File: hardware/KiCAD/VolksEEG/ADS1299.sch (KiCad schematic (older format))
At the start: 18 parts, among them U1 ADS1299IPAG

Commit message: Added Digi-key's kicad component libraries, some work done on power, think this will change but capturing it here for posterity.
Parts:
- removed C? (x4): 100n, symbol Device:C
- removed C? (x6): 1u, symbol Device:C
- removed R?: 10k, symbol Device:R
- added C? (x2): 100n, symbol Device:C
- added C? (x4): 1u, symbol Device:C
- added C?: 0.1u, symbol Device:C
- added C?: 10u, symbol Device:C
- added R? (x2): ?, symbol Device:R
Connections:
- net labels added: +2V5, -2V5, MISO_ads, MOSI_ads, SCK_ads, nCS_ads, nDRDY_ads
- net labels removed: MISO, MOSI, SCK, nCS
- wire segments 107 -> 91

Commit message: Updating analogue inputs to the referential montage and connected a few ADS1299 pins.
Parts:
- added R? (x2): 10K, symbol Device:R
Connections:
- net labels added: AIN1, AIN2, AIN3, AIN4, AIN5, AIN6, AIN7, AIN8, BIAS_INV, BIAS_OUT, REF, VDD
- net labels removed: AIN1N, AIN1P, AIN2N, AIN2P, AIN3N, AIN3P, AIN4N, AIN4P, AIN5N, AIN5P, AIN6N, AIN6P, AIN7N, AIN7P, AIN8N, AIN8P
- wire segments 91 -> 110
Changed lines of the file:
@@
 Wire Wire Line
 	5550 4250 6000 4250
-Text HLabel 3550 1500 0    50   Input ~ 0
+Text HLabel 3500 1500 0    50   Input ~ 0
 ADS-nRST
-Text HLabel 3500 3250 0    50   Input ~ 0
-AIN5N
 Text HLabel 3500 3350 0    50   Input ~ 0
-AIN5P
-Text HLabel 3500 3450 0    50   Input ~ 0
-AIN6N
+AIN5
 Text HLabel 3500 3550 0    50   Input ~ 0
-AIN6P
-Text HLabel 3500 3650 0    50   Input ~ 0
-AIN7N
+AIN6
 Text HLabel 3500 3750 0    50   Input ~ 0
-AIN7P
-Text HLabel 3500 3850 0    50   Input ~ 0
-AIN8N
+AIN7
 Text HLabel 3500 3950 0    50   Input ~ 0
-AIN8P
+AIN8
 Wire Wire Line
 	3500 4250 4150 4250
@@
 	4150 3950 3500 3950
 Wire Wire Line
-	4150 3850 3500 3850
-Wire Wire Line
 	4150 3750 3500 3750
 Wire Wire Line
-	4150 3650 3500 3650
-Wire Wire Line
 	3500 3550 4150 3550
 Wire Wire Line
-	4150 3450 3500 3450
-Wire Wire Line
 	3500 3350 4150 3350
-Wire Wire Line
-	4150 3250 3500 3250
-Text HLabel 3500 2450 0    50   Input ~ 0
-AIN1N
 Text HLabel 3500 2550 0    50   Input ~ 0
-AIN1P
-Text HLabel 3500 2650 0    50   Input ~ 0
-AIN2N
+AIN1
 Text HLabel 3500 2750 0    50   Input ~ 0
-AIN2P
-Text HLabel 3500 2850 0    50   Input ~ 0
-AIN3N
+AIN2
 Text HLabel 3500 2950 0    50   Input ~ 0
-AIN3P
-Text HLabel 3500 3050 0    50   Input ~ 0
-AIN4N
+AIN3
 Text HLabel 3500 3150 0    50   Input ~ 0
-AIN4P
+AIN4
 Wire Wire Line
 	4150 3150 3500 3150
 Wire Wire Line
-	4150 3050 3500 3050
-Wire Wire Line
 	4150 2950 3500 2950
 Wire Wire Line
-	4150 2850 3500 2850
-Wire Wire Line
 	3500 2750 4150 2750
 Wire Wire Line
-	4150 2650 3500 2650
-Wire Wire Line
 	3500 2550 4150 2550
-Wire Wire Line
-	4150 2450 3500 2450
 Wire Wire Line
 	5550 1750 5550 1650
@@
 Text HLabel 6800 2250 2    50   Output ~ 0
 nDRDY_ads
-$Comp
-L power:+3V3 #PWR?
-U 1 1 617DA57B
-P 6650 1500
-F 0 "#PWR?" H 6650 1350 50  0001 C CNN
-F 1 "+3V3" V 6665 1628 50  0000 L CNN
-F 2 "" H 6650 1500 50  0001 C CNN
-F 3 "" H 6650 1500 50  0001 C CNN
-	1    6650 1500
-	1    0    0    -1
-$EndComp
 Wire Wire Line
 	5900 2000 5900 1800
@@
 Connection ~ 6650 2250
 Wire Wire Line
-	3550 1500 4150 1500
+	3500 1500 4150 1500
 Wire Wire Line
 	6650 1500 6650 1600
@@
 Text HLabel 6550 6000 2    50   Input ~ 0
 -2V5
+$Comp
+L power:VDD #PWR?
+U 1 1 61A7B2BC
+P 6650 1500
+AR Path="/615BA255/61A7B2BC" Ref="#PWR?"  Part="1"
+AR Path="/615BA110/61A7B2BC" Ref="#PWR?"  Part="1"
+F 0 "#PWR?" H 6650 1350 50  0001 C CNN
+F 1 "VDD" H 6665 1673 50  0000 C CNN
+F 2 "" H 6650 1500 50  0001 C CNN
+F 3 "" H 6650 1500 50  0001 C CNN
+	1    6650 1500
+	1    0    0    -1
+$EndComp
+$Comp
+L Device:R R?
+U 1 1 61A7F38E
+P 3850 1750
+F 0 "R?" V 3950 1650 50  0000 L CNN
+F 1 "10K" V 3950 1800 50  0000 L CNN
+F 2 "" V 3780 1750 50  0001 C CNN
+F 3 "~" H 3850 1750 50  0001 C CNN
+	1    3850 1750
+	0    -1   -1   0
+$EndComp
+$Comp
+L power:VDD #PWR?
+U 1 1 61A7F869
+P 2750 1550
+AR Path="/615BA255/61A7F869" Ref="#PWR?"  Part="1"
+AR Path="/615BA110/61A7F869" Ref="#PWR?"  Part="1"
+F 0 "#PWR?" H 2750 1400 50  0001 C CNN
+F 1 "VDD" H 2765 1723 50  0000 C CNN
+F 2 "" H 2750 1550 50  0001 C CNN
+F 3 "" H 2750 1550 50  0001 C CNN
+	1    2750 1550
+	1    0    0    -1
+$EndComp
+Wire Wire Line
+	2750 1550 2750 1750
+Wire Wire Line
+	2750 1750 3700 1750
+Wire Wire Line
+	4000 1750 4150 1750
+Text HLabel 5850 2350 2    50   Output ~ 0
+BIAS_OUT
+Text HLabel 3500 2100 0    50   Output ~ 0
+BIAS_INV
+Wire Wire Line
+	3500 2100 4150 2100
+Wire Wire Line
+	5550 2350 5850 2350
+$Comp
+L Device:R R?
+U 1 1 61AF48E0
+P 3850 1400
+F 0 "R?" V 3950 1300 50  0000 L CNN
+F 1 "10K" V 3950 1450 50  0000 L CNN
+F 2 "" V 3780 1400 50  0001 C CNN
+F 3 "~" H 3850 1400 50  0001 C CNN
+	1    3850 1400
+	0    -1   -1   0
+$EndComp
+$Comp
+L power:VDD #PWR?
+U 1 1 61AF7617
+P 3500 1200
+AR Path="/615BA255/61AF7617" Ref="#PWR?"  Part="1"
+AR Path="/615BA110/61AF7617" Ref="#PWR?"  Part="1"
+F 0 "#PWR?" H 3500 1050 50  0001 C CNN
+F 1 "VDD" H 3515 1373 50  0000 C CNN
+F 2 "" H 3500 1200 50  0001 C CNN
+F 3 "" H 3500 1200 50  0001 C CNN
+	1    3500 1200
+	1    0    0    -1
+$EndComp
+Wire Wire Line
+	3500 1200 3500 1400
+Wire Wire Line
+	3500 1400 3700 1400
+Wire Wire Line
+	4000 1400 4150 1400
+Text HLabel 3500 5600 0    50   Input ~ 0
+REF
+Wire Wire Line
+	3500 5600 4150 5600
+$Comp
+L power:VDD #PWR?
+U 1 1 61B0BA08
+P 2750 2400
+AR Path="/615BA255/61B0BA08" Ref="#PWR?"  Part="1"
+AR Path="/615BA110/61B0BA08" Ref="#PWR?"  Part="1"
+F 0 "#PWR?" H 2750 2250 50  0001 C CNN
+F 1 "VDD" H 2765 2573 50  0000 C CNN
+F 2 "" H 2750 2400 50  0001 C CNN
+F 3 "" H 2750 2400 50  0001 C CNN
+	1    2750 2400
+	1    0    0    -1
+$EndComp
+Wire Wire Line
+	2750 2400 2750 2450
+Wire Wire Line
+	2750 3850 4150 3850
+Wire Wire Line
+	4150 3650 2750 3650
+Connection ~ 2750 3650
+Wire Wire Line
+	2750 3650 2750 3850
+Wire Wire Line
+	4150 3450 2750 3450
+Connection ~ 2750 3450
+Wire Wire Line
+	2750 3450 2750 3650
+Wire Wire Line
+	2750 3250 4150 3250
+Connection ~ 2750 3250
+Wire Wire Line
+	2750 3250 2750 3450
+Wire Wire Line
+	4150 3050 2750 3050
+Connection ~ 2750 3050
+Wire Wire Line
+	2750 3050 2750 3250
+Wire Wire Line
+	2750 2850 4150 2850
+Connection ~ 2750 2850
+Wire Wire Line
+	2750 2850 2750 3050
+Wire Wire Line
+	2750 2650 4150 2650
+Connection ~ 2750 2650
+Wire Wire Line
+	2750 2650 2750 2850
+Wire Wire Line
+	2750 2450 4150 2450
+Connection ~ 2750 2450
+Wire Wire Line
+	2750 2450 2750 2650
+$Comp
+L power:GNDA #PWR?
+U 1 1 61B27A78
+P 2950 1950
+F 0 "#PWR?" H 2950 1700 50  0001 C CNN
+F 1 "GNDA" H 2955 1777 50  0000 C CNN
+F 2 "" H 2950 1950 50  0001 C CNN
+F 3 "" H 2950 1950 50  0001 C CNN
+	1    2950 1950
+	1    0    0    -1
+$EndComp
+Wire Wire Line
+	2950 1950 2950 1850
+Wire Wire Line
+	2950 1850 4150 1850
 $EndSCHEMATC

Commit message: Updated names of heirarchical pins, finished referential montage configuration, added filter cap to ADS_nRST line, started putting ADS1299 gpios to a header.
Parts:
- removed U?: OPA388IDGKR, VolksEEG:SOP65P490X110-8N, symbol VolksEEG:OPA388IDGKR
- added C?: 100n, symbol Device:C
- added R?: 10K, symbol Device:R
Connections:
- net labels added: ADS_nDRDY, ADS_nRST, MISO, MOSI, SCK, nCS
- net labels removed: ADS-nRST, MISO_ads, MOSI_ads, SCK_ads, nCS_ads, nDRDY_ads
- wire segments 110 -> 125
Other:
- moved on the sheet: R?
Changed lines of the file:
@@
 $EndComp
 Text HLabel 3500 4250 0    50   Input ~ 0
-nCS_ads
+nCS
 Text HLabel 3500 4350 0    50   Input ~ 0
-SCK_ads
+SCK
 Text HLabel 3500 4450 0    50   Input ~ 0
-MOSI_ads
+MOSI
 Text HLabel 6000 4250 2    50   Output ~ 0
-MISO_ads
+MISO
 Wire Wire Line
 	5550 4250 6000 4250
-Text HLabel 3500 1500 0    50   Input ~ 0
-ADS-nRST
+Text HLabel 3300 1500 0    50   Input ~ 0
+ADS_nRST
 Text HLabel 3500 3350 0    50   Input ~ 0
 AIN5
@@
 Wire Wire Line
 	7500 5400 7500 5300
-$Comp
-L VolksEEG:OPA388IDGKR U?
-U 1 1 617AA68D
-P 8650 3600
-F 0 "U?" H 8994 3646 50  0000 L CNN
-F 1 "OPA388IDGKR" H 8994 3555 50  0000 L CNN
-F 2 "VolksEEG:SOP65P490X110-8N" H 8650 3600 50  0001 C CNN
-F 3 "https://www.ti.com/lit/gpn/opa388" H 8650 3600 50  0001 C CNN
-	1    8650 3600
-	1    0    0    -1
-$EndComp
 Wire Wire Line
 	5550 2550 5700 2550
@@
 $EndComp
 Text HLabel 6800 2250 2    50   Output ~ 0
-nDRDY_ads
+ADS_nDRDY
 Wire Wire Line
 	5900 2000 5900 1800
@@
 Connection ~ 6650 2250
 Wire Wire Line
-	3500 1500 4150 1500
+	3300 1500 3550 1500
 Wire Wire Line
 	6650 1500 6650 1600
@@
 L Device:R R?
 U 1 1 61A7F38E
-P 3850 1750
-F 0 "R?" V 3950 1650 50  0000 L CNN
-F 1 "10K" V 3950 1800 50  0000 L CNN
-F 2 "" V 3780 1750 50  0001 C CNN
-F 3 "~" H 3850 1750 50  0001 C CNN
-	1    3850 1750
-	0    -1   -1   0
-$EndComp
-$Comp
-L power:VDD #PWR?
-U 1 1 61A7F869
-P 2750 1550
-AR Path="/615BA255/61A7F869" Ref="#PWR?"  Part="1"
-AR Path="/615BA110/61A7F869" Ref="#PWR?"  Part="1"
-F 0 "#PWR?" H 2750 1400 50  0001 C CNN
-F 1 "VDD" H 2765 1723 50  0000 C CNN
-F 2 "" H 2750 1550 50  0001 C CNN
-F 3 "" H 2750 1550 50  0001 C CNN
-	1    2750 1550
-	1    0    0    -1
-$EndComp
-Wire Wire Line
-	2750 1550 2750 1750
-Wire Wire Line
-	2750 1750 3700 1750
-Wire Wire Line
-	4000 1750 4150 1750
+P 4050 1000
+F 0 "R?" V 4150 900 50  0000 L CNN
+F 1 "10K" V 4150 1050 50  0000 L CNN
+F 2 "" V 3980 1000 50  0001 C CNN
+F 3 "~" H 4050 1000 50  0001 C CNN
+	1    4050 1000
+	-1   0    0    1
+$EndComp
 Text HLabel 5850 2350 2    50   Output ~ 0
 BIAS_OUT
@@
 L Device:R R?
 U 1 1 61AF48E0
-P 3850 1400
-F 0 "R?" V 3950 1300 50  0000 L CNN
-F 1 "10K" V 3950 1450 50  0000 L CNN
-F 2 "" V 3780 1400 50  0001 C CNN
-F 3 "~" H 3850 1400 50  0001 C CNN
-	1    3850 1400
-	0    -1   -1   0
+P 3800 1000
+F 0 "R?" V 3900 900 50  0000 L CNN
+F 1 "10K" V 3900 1050 50  0000 L CNN
+F 2 "" V 3730 1000 50  0001 C CNN
+F 3 "~" H 3800 1000 50  0001 C CNN
+	1    3800 1000
+	-1   0    0    1
 $EndComp
 $Comp
 L power:VDD #PWR?
 U 1 1 61AF7617
-P 3500 1200
+P 3800 700
 AR Path="/615BA255/61AF7617" Ref="#PWR?"  Part="1"
 AR Path="/615BA110/61AF7617" Ref="#PWR?"  Part="1"
-F 0 "#PWR?" H 3500 1050 50  0001 C CNN
-F 1 "VDD" H 3515 1373 50  0000 C CNN
-F 2 "" H 3500 1200 50  0001 C CNN
-F 3 "" H 3500 1200 50  0001 C CNN
-	1    3500 1200
-	1    0    0    -1
-$EndComp
-Wire Wire Line
-	3500 1200 3500 1400
-Wire Wire Line
-	3500 1400 3700 1400
-Wire Wire Line
-	4000 1400 4150 1400
+F 0 "#PWR?" H 3800 550 50  0001 C CNN
+F 1 "VDD" H 3815 873 50  0000 C CNN
+F 2 "" H 3800 700 50  0001 C CNN
+F 3 "" H 3800 700 50  0001 C CNN
+	1    3800 700
+	1    0    0    -1
+$EndComp
 Text HLabel 3500 5600 0    50   Input ~ 0
 REF
@@
 	2950 1950 2950 1850
 Wire Wire Line
-	2950 1850 4150 1850
+	2950 1850 3550 1850
+Entry Wire Line
+	3950 5450 4050 5350
+Entry Wire Line
+	3850 5450 3950 5350
+Entry Wire Line
+	3750 5450 3850 5350
+Entry Wire Line
+	3650 5450 3750 5350
+Wire Wire Line
+	4050 5350 4150 5350
+Wire Wire Line
+	4150 5250 4050 5250
+Wire Wire Line
+	4050 5250 3950 5350
+Wire Wire Line
+	4050 5150 3850 5350
+Wire Wire Line
+	4150 5150 4050 5150
+Wire Wire Line
+	3750 5350 4050 5050
+Wire Wire Line
+	4050 5050 4150 5050
+$Comp
+L Device:R R?
+U 1 1 61B84C6B
+P 3550 1000
+F 0 "R?" V 3650 900 50  0000 L CNN
+F 1 "10K" V 3650 1050 50  0000 L CNN
+F 2 "" V 3480 1000 50  0001 C CNN
+F 3 "~" H 3550 1000 50  0001 C CNN
+	1    3550 1000
+	-1   0    0    1
+$EndComp
+Wire Wire Line
+	3550 850  3550 750
+Wire Wire Line
+	3550 750  3800 750
+Wire Wire Line
+	3800 750  3800 700
+Wire Wire Line
+	3800 850  3800 750
+Connection ~ 3800 750
+Wire Wire Line
+	4050 850  4050 750
+Wire Wire Line
+	4050 750  3800 750
+Wire Wire Line
+	3550 1150 3550 1500
+Connection ~ 3550 1500
+Wire Wire Line
+	3550 1500 4150 1500
+Wire Wire Line
+	4050 1150 4050 1400
+Wire Wire Line
+	4050 1400 4150 1400
+Wire Wire Line
+	3800 1150 3800 1750
+Wire Wire Line
+	3800 1750 4150 1750
+$Comp
+L Device:C C?
+U 1 1 61B9DFC8
+P 3550 1650
+AR Path="/615BA110/61B9DFC8" Ref="C?"  Part="1"
+AR Path="/615BA255/61B9DFC8" Ref="C?"  Part="1"
+F 0 "C?" V 3700 1750 50  0000 L CNN
+F 1 "100n" V 3700 1500 50  0000 L CNN
+F 2 "" H 3588 1500 50  0001 C CNN
+F 3 "~" H 3550 1650 50  0001 C CNN
+	1    3550 1650
+	-1   0    0    1
+$EndComp
+Wire Wire Line
+	3550 1800 3550 1850
+Wire Bus Line
+	1650 5450 3950 5450
+Connection ~ 3550 1850
+Wire Wire Line
+	3550 1850 4150 1850
 $EndSCHEMATC

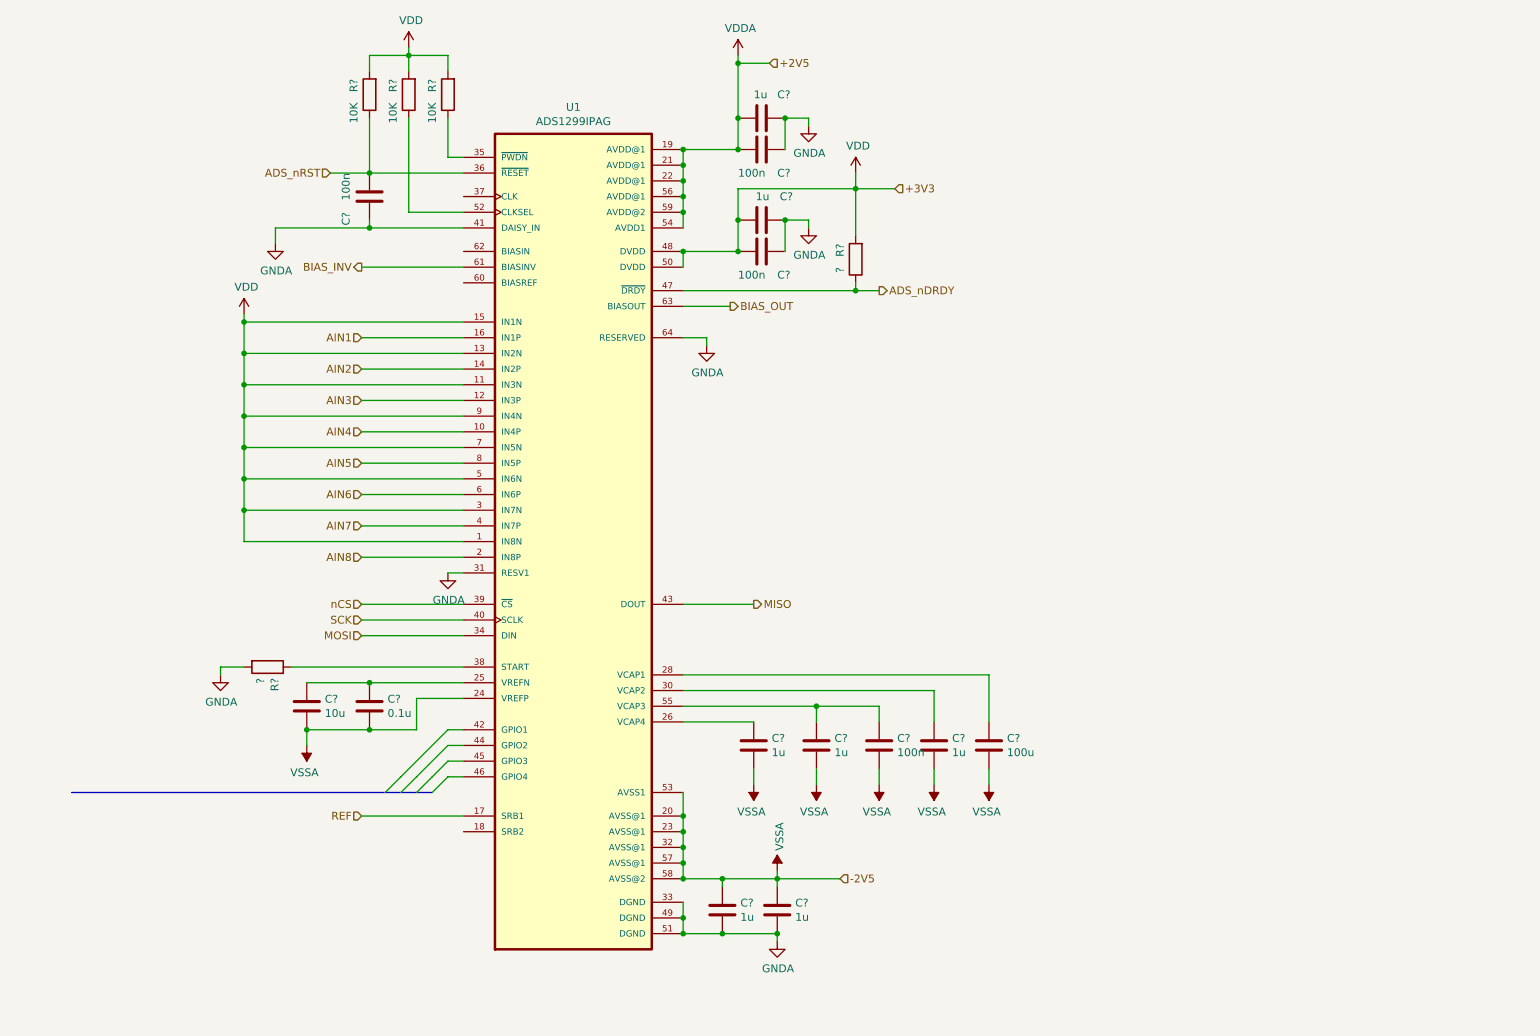
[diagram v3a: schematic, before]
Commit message: Added custom power symbols for non isolated power. Seperated Analogue and digital supplies. finished putting the ADS1299 GPIOs to a header.
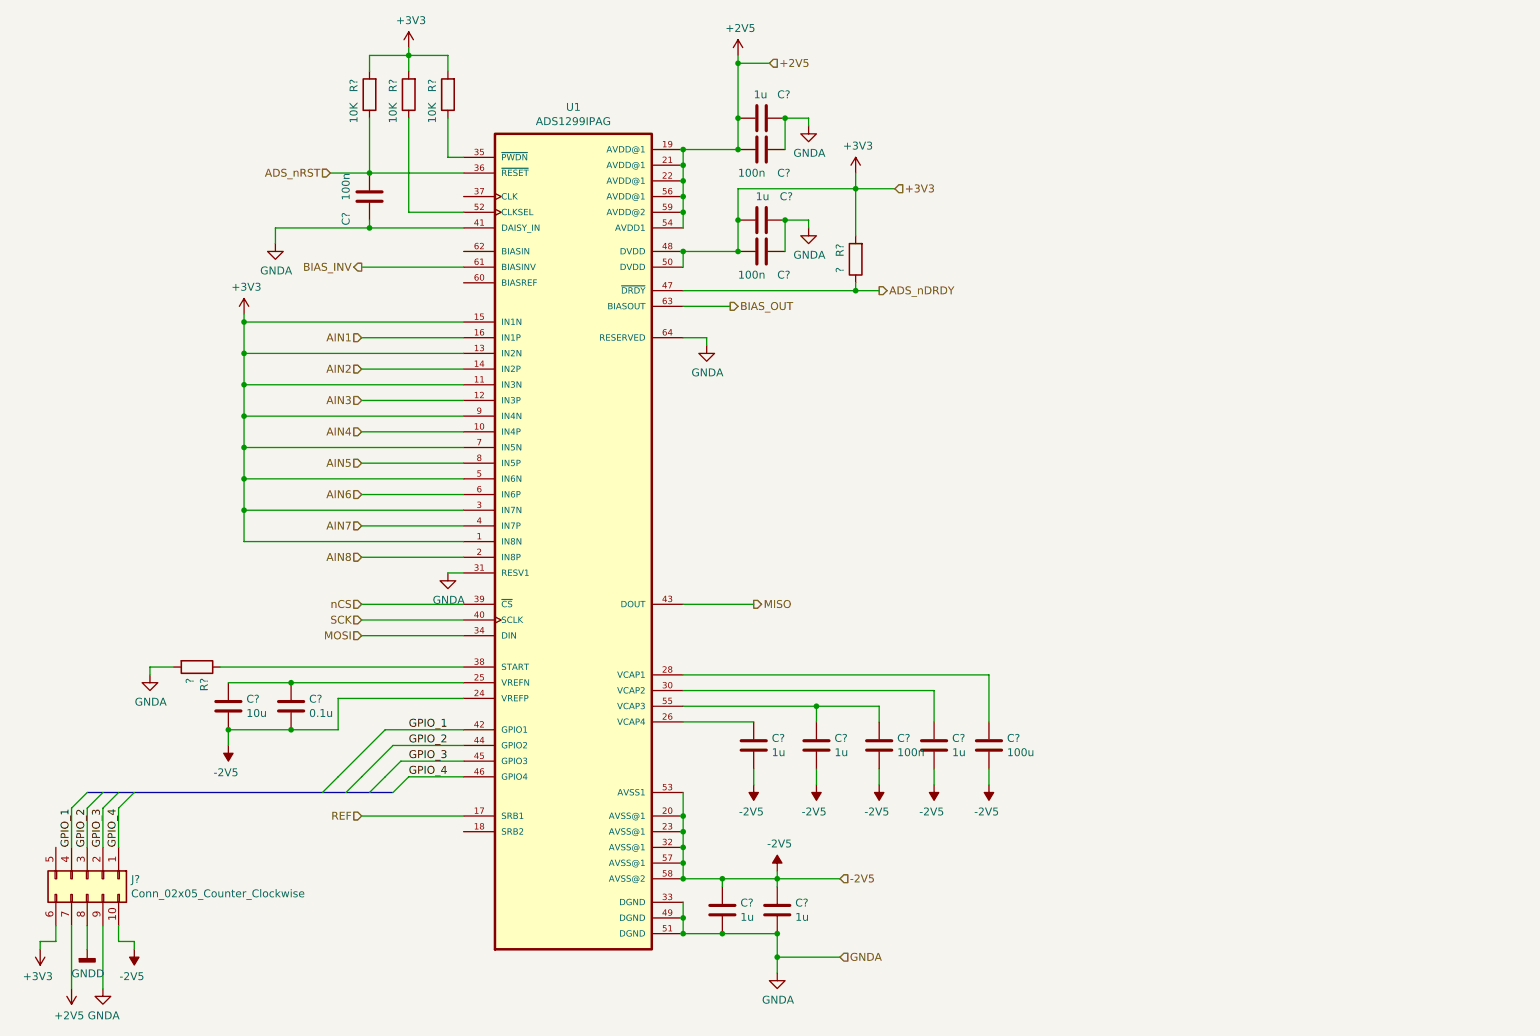
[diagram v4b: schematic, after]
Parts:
- added J?: Conn_02x05_Counter_Clockwise, symbol Connector_Generic:Conn_02x05_Counter_Clockwise
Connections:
- net GNDA: now also J?.9 (Pin_9)
- net GPIO_1: now reaches U1.42 (GPIO1)
- net GPIO_1: now also J?.4 (Pin_4)
- net GPIO_2: now reaches U1.44 (GPIO2)
- net GPIO_2: now also J?.3 (Pin_3)
- net GPIO_3: now reaches U1.45 (GPIO3)
- net GPIO_3: now also J?.2 (Pin_2)
- net GPIO_4: now reaches U1.46 (GPIO4)
- net GPIO_4: now also J?.1 (Pin_1)
- net VDD renamed +3V3
- net +3V3: now also J?.6 (Pin_6)
- net VDDA renamed +2V5
- net +2V5: now also J?.7 (Pin_7)
- net VSSA renamed -2V5
- net -2V5: now also J?.10 (Pin_10)
- new net GNDD: J?.8 (Pin_8)
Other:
- moved on the sheet: C?, R?

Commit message: Tweaks based on feedback, Changed digital isolators to ADUM240E devices due to component availability.
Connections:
- net GNDD is gone; now on net GNDA: J?.8 (Pin_8)
- net +2V5: now also U1.1 (IN8N), U1.11 (IN3N), U1.13 (IN2N), U1.15 (IN1N), U1.3 (IN7N), U1.5 (IN6N), U1.7 (IN5N), U1.9 (IN4N)
- net +3V3: no longer U1.1 (IN8N), U1.11 (IN3N), U1.13 (IN2N), U1.15 (IN1N), U1.3 (IN7N), U1.5 (IN6N), U1.7 (IN5N), U1.9 (IN4N)
- net -2V5: now also C?.1, C?.1, U1.25 (VREFN); no longer C?.2, C?.2, U1.24 (VREFP)
- new net: C?.2, C?.2, U1.24 (VREFP)
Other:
- moved on the sheet: R?
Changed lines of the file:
@@
 $Descr A4 11693 8268
 encoding utf-8
-Sheet 2 6
+Sheet 6 6
 Title ""
 Date ""
@@
 L Device:R R?
 U 1 1 61760E4E
-P 2450 4650
-F 0 "R?" H 2520 4696 50  0000 L CNN
-F 1 "?" H 2520 4605 50  0000 L CNN
-F 2 "" V 2380 4650 50  0001 C CNN
-F 3 "~" H 2450 4650 50  0001 C CNN
-	1    2450 4650
+P 2050 4650
+F 0 "R?" H 2120 4696 50  0000 L CNN
+F 1 "?" H 2120 4605 50  0000 L CNN
+F 2 "" V 1980 4650 50  0001 C CNN
+F 3 "~" H 2050 4650 50  0001 C CNN
+	1    2050 4650
 	0    1    1    0
 $EndComp
@@
 L power:GNDA #PWR?
 U 1 1 6176CAC2
-P 2150 4700
-F 0 "#PWR?" H 2150 4450 50  0001 C CNN
-F 1 "GNDA" H 2155 4527 50  0000 C CNN
-F 2 "" H 2150 4700 50  0001 C CNN
-F 3 "" H 2150 4700 50  0001 C CNN
-	1    2150 4700
-	1    0    0    -1
-$EndComp
-Wire Wire Line
-	2150 4700 2150 4650
-Wire Wire Line
-	2150 4650 2300 4650
+P 1750 4700
+F 0 "#PWR?" H 1750 4450 50  0001 C CNN
+F 1 "GNDA" H 1755 4527 50  0000 C CNN
+F 2 "" H 1750 4700 50  0001 C CNN
+F 3 "" H 1750 4700 50  0001 C CNN
+	1    1750 4700
+	1    0    0    -1
+$EndComp
+Wire Wire Line
+	1750 4700 1750 4650
+Wire Wire Line
+	1750 4650 1900 4650
 $Comp
 L Device:C C?
@@
 	3350 4850 4150 4850
 Wire Wire Line
-	2650 5150 2650 5050
-Wire Wire Line
 	2650 5050 3050 5050
-Connection ~ 2650 5050
 Wire Wire Line
 	3350 5050 3050 5050
@@
 	1650 5550 1650 5800
 Wire Wire Line
-	2600 4650 4150 4650
+	2200 4650 4150 4650
 Wire Wire Line
 	3050 4750 4150 4750
@@
 	1    0    0    -1
 $EndComp
-Text HLabel 6550 6500 2    50   Input ~ 0
+Text HLabel 5850 2550 2    50   Input ~ 0
 GNDA
 Wire Wire Line
@@
 $EndComp
 $Comp
-L power:+3V3 #PWR?
-U 1 1 61C85B3F
-P 2750 2400
-F 0 "#PWR?" H 2750 2250 50  0001 C CNN
-F 1 "+3V3" H 2765 2573 50  0000 C CNN
-F 2 "" H 2750 2400 50  0001 C CNN
-F 3 "" H 2750 2400 50  0001 C CNN
-	1    2750 2400
-	1    0    0    -1
-$EndComp
-$Comp
 L power:-2V5 #PWR?
 U 1 1 61C86288
@@
 L power:-2V5 #PWR?
 U 1 1 61C86FED
-P 2650 5150
-F 0 "#PWR?" H 2650 5250 50  0001 C CNN
-F 1 "-2V5" H 2665 5323 50  0000 C CNN
-F 2 "" H 2650 5150 50  0001 C CNN
-F 3 "" H 2650 5150 50  0001 C CNN
-	1    2650 5150
+P 2400 4900
+F 0 "#PWR?" H 2400 5000 50  0001 C CNN
+F 1 "-2V5" H 2415 5073 50  0000 C CNN
+F 2 "" H 2400 4900 50  0001 C CNN
+F 3 "" H 2400 4900 50  0001 C CNN
+	1    2400 4900
 	-1   0    0    1
 $EndComp
@@
 Wire Wire Line
 	1850 6700 1850 6300
+Wire Wire Line
+	2650 4750 2400 4750
+Wire Wire Line
+	2400 4750 2400 4900
+Connection ~ 2650 4750
+$Comp
+L power:+2V5 #PWR?
+U 1 1 61CCB2FD
+P 2750 2400
+F 0 "#PWR?" H 2750 2250 50  0001 C CNN
+F 1 "+2V5" H 2765 2573 50  0000 C CNN
+F 2 "" H 2750 2400 50  0001 C CNN
+F 3 "" H 2750 2400 50  0001 C CNN
+	1    2750 2400
+	1    0    0    -1
+$EndComp
+Wire Wire Line
+	5700 2550 5850 2550
+Connection ~ 5700 2550
+Text HLabel 6550 6500 2    50   Input ~ 0
+GNDD
 Wire Bus Line
 	1750 5450 3700 5450
